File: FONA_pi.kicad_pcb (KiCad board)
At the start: 2 copper layers, 88.4 x 59.1 mm, 35 parts, among them J1 Conn_01x20_Socket, J10 Conn_01x04_Pin, J11 Conn_01x20_Socket, J12 Conn_01x20_Socket, J13 Conn_01x06_Socket, J14 Conn_01x06_Socket, J15 Conn_01x06_Socket, J3 Conn_01x20_Socket, J4 Conn_01x20_Socket, J5 Conn_01x18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

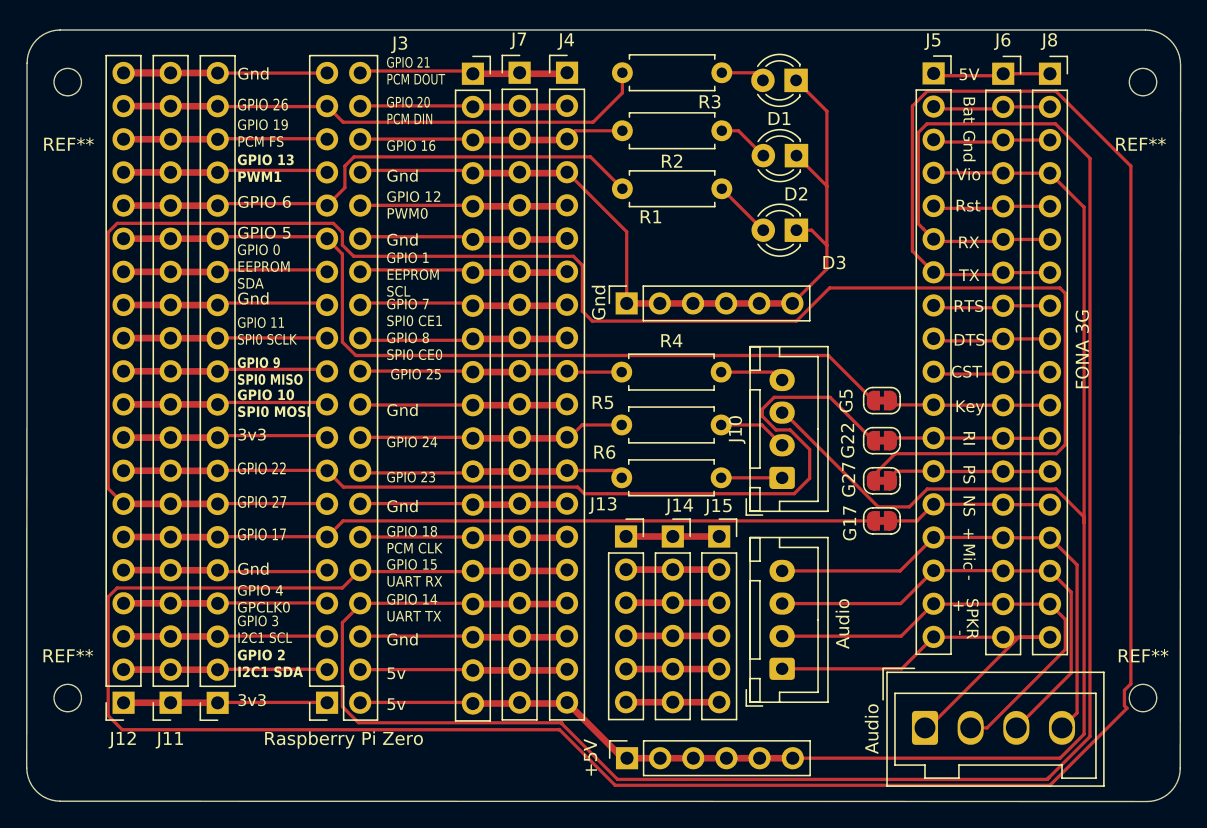
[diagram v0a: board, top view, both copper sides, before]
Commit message: Had to reposition a lot after pulling in from schematic
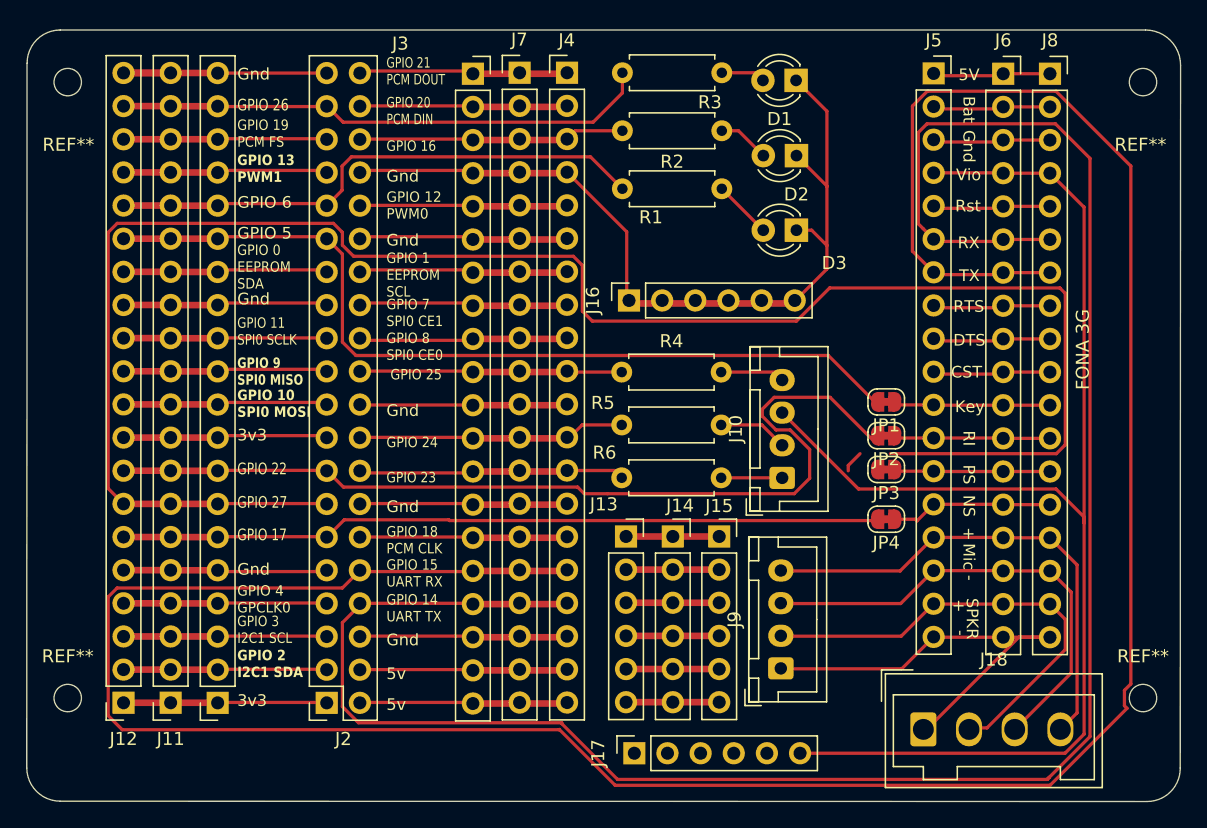
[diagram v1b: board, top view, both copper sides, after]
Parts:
- removed +5V, Gnd: Conn_01x06_Socket, Connector_PinSocket_2.54mm:PinSocket_1x06_P2.54mm_Vertical
- removed Audio: Conn_01x04, Connector_Wago:Wago_734-134_1x04_P3.50mm_Vertical
- removed Audio: Conn_01x04_Pin, Connector_JST:JST_XH_B4B-XH-A_1x04_P2.50mm_Vertical
- removed G17, G22, G27, G5: J2B, Jumper:SolderJumper-2_P1.3mm_Bridged_RoundedPad1.0x1.5mm
- removed Raspberry Pi Zero: Conn_02x20_Odd_Even, Connector_PinSocket_2.54mm:PinSocket_2x20_P2.54mm_Vertical
- added J16: Conn_01x06_Socket, Connector_PinSocket_2.54mm:PinSocket_1x06_P2.54mm_Vertical, F.Cu at (124.6, 78.3)
- added J17: Conn_01x06_Socket, Connector_PinSocket_2.54mm:PinSocket_1x06_P2.54mm_Vertical, F.Cu at (125.0, 113.0)
- added J18: Conn_01x04, Connector_Wago:Wago_734-134_1x04_P3.50mm_Vertical, F.Cu at (147.2, 111.2)
- added J2: Conn_02x20_Odd_Even, Connector_PinSocket_2.54mm:PinSocket_2x20_P2.54mm_Vertical, F.Cu at (101.4, 109.2)
- added J9: Conn_01x04_Pin, Connector_JST:JST_XH_B4B-XH-A_1x04_P2.50mm_Vertical, F.Cu at (136.2, 106.5)
- added JP1: J2B, Jumper:SolderJumper-2_P1.3mm_Bridged_RoundedPad1.0x1.5mm, F.Cu at (144.3, 86.1)
- added JP2: J2B, Jumper:SolderJumper-2_P1.3mm_Bridged_RoundedPad1.0x1.5mm, F.Cu at (144.3, 88.7)
- added JP3: J2B, Jumper:SolderJumper-2_P1.3mm_Bridged_RoundedPad1.0x1.5mm, F.Cu at (144.3, 91.3)
- added JP4: J2B, Jumper:SolderJumper-2_P1.3mm_Bridged_RoundedPad1.0x1.5mm, F.Cu at (144.3, 95.1)
- J8: value unk -> Conn_01x18
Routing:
- net Net-(J10-Pin_3): track 139.3 -> 118.2 mm
- net Net-(J5-Pin_13): track 12.8 -> 11.8 mm
- net Net-(J1-Pin_7): track 145.4 -> 144.7 mm
- net Net-(J5-Pin_14): track 13.0 -> 12.5 mm

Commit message: Fixed DRC violations
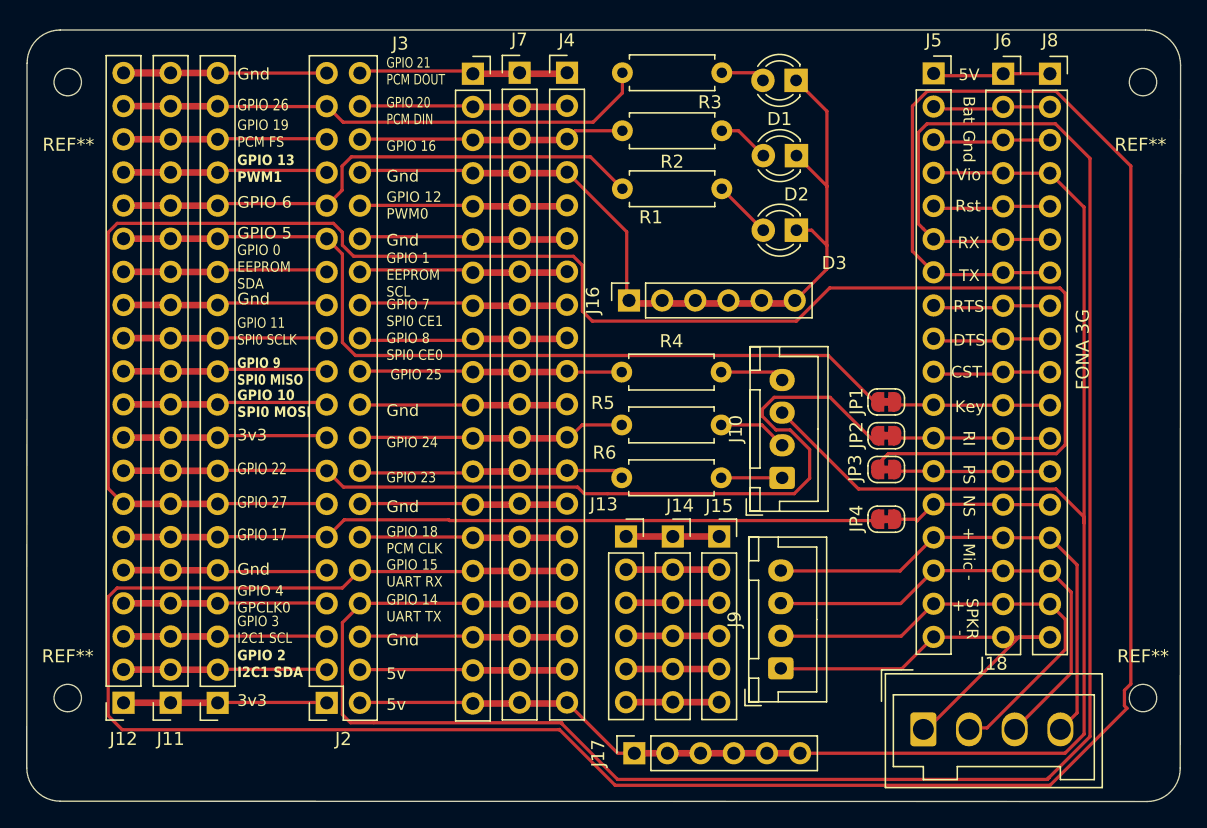
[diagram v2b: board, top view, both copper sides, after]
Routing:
- net Net-(J10-Pin_3): track 118.2 -> 137.6 mm

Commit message: last commit didn't have some saved files that are in this commit
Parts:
- J9 Audio: renamed from J9
- renumbered J16 to GND
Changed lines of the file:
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@@
     (property "ki_keywords" "connector")
     (attr through_hole)
-    (fp_text reference "J9" (at 3.75 -3.55 90) (layer "F.SilkS")
+    (fp_text reference "J9 Audio" (at -3.556 0 180) (layer "F.SilkS")
         (effects (font (size 1 1) (thickness 0.15)))
     )
@@
     (property "ki_keywords" "connector")
     (attr through_hole)
-    (fp_text reference "J16" (at 0 -2.77 90) (layer "F.SilkS")
-        (effects (font (size 1 1) (thickness 0.15)))
-    )
+    (fp_text reference "GND" (at 0 -2.4384 90) (layer "F.SilkS")
+        (effects (font (size 1 1) (thickness 0.15)))
+    )

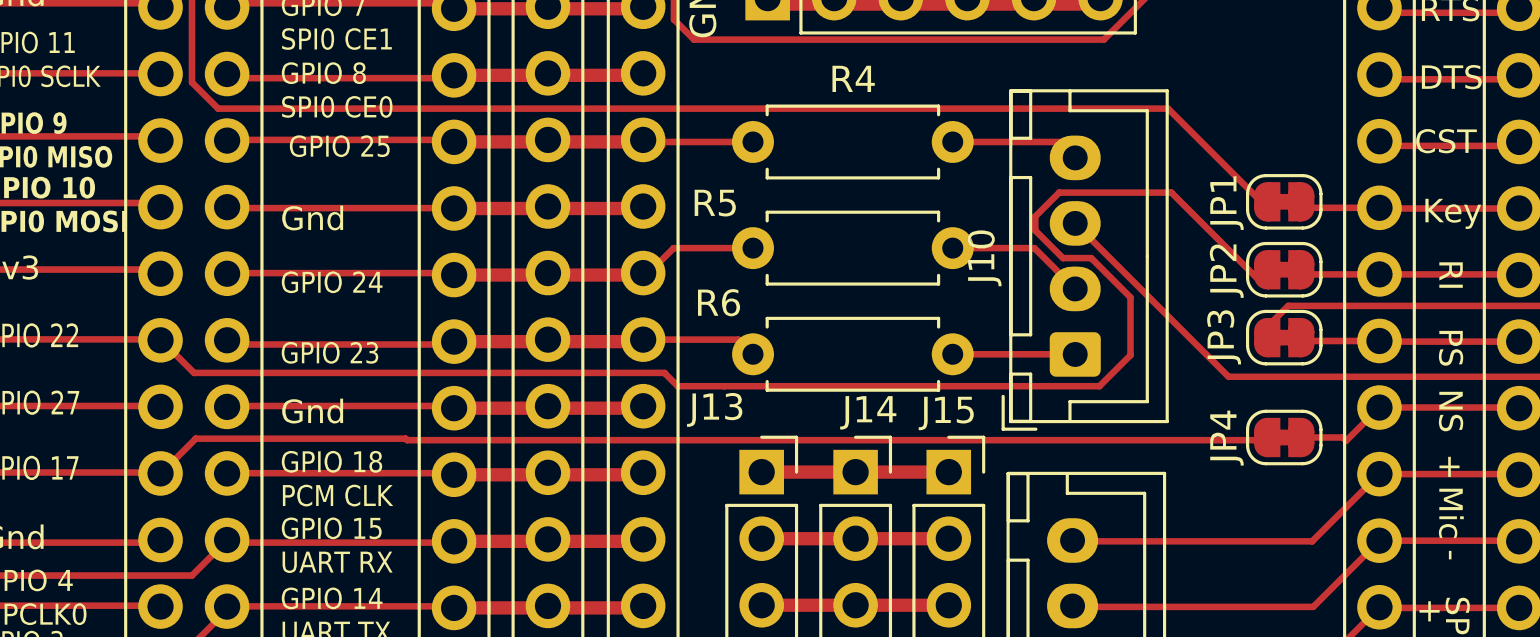
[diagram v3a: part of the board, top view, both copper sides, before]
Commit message: Rearranged jumper pads and tracks
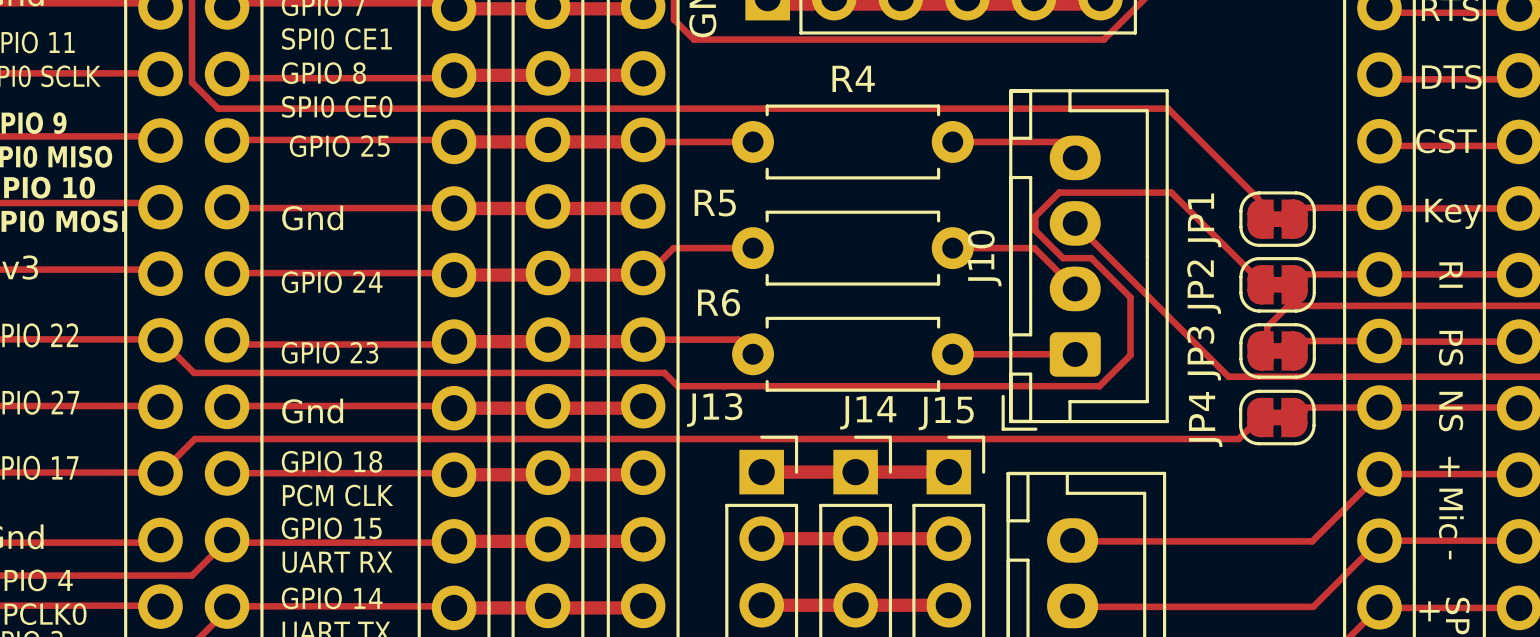
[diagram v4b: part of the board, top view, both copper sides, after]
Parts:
- moved JP4 0.81 mm to (144.1, 94.3)
- moved JP1 0.71 mm to (144.1, 86.8)
- moved JP2 0.63 mm to (144.1, 89.3)
- moved JP3 0.57 mm to (144.1, 91.8)
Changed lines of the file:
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@@
   )
   (footprint "Jumper:SolderJumper-2_P1.3mm_Bridged_RoundedPad1.0x1.5mm" (layer "F.Cu")
-    (at 144.3228 88.6968 180)
+    (at 144.0688 89.272533 180)
     (descr "SMD Solder Jumper, 1x1.5mm, rounded Pads, 0.3mm gap, bridged with 1 copper strip")
     (tags "net tie solder jumper bridged")
@@
     (attr exclude_from_pos_files)
     (net_tie_pad_groups "1, 2")
-    (fp_text reference "JP2" (at 2.286 0.0508 90) (layer "F.SilkS")
-        (effects (font (size 1 1) (thickness 0.15)))
-    )
-    (fp_text value "J2B" (at 0 1.9) (layer "F.Fab")
+    (fp_text reference "JP2" (at 2.8956 0.016933 90) (layer "F.SilkS")
+        (effects (font (size 1 1) (thickness 0.15)))
+    )
+    (fp_text value "J2B" (at 2.4384 1.998133) (layer "F.Fab")
         (effects (font (size 1 1) (thickness 0.15)))
     )
@@
   )
   (footprint "Jumper:SolderJumper-2_P1.3mm_Bridged_RoundedPad1.0x1.5mm" (layer "F.Cu")
-    (at 144.3228 95.0976 180)
+    (at 144.0584 94.3356 180)
     (descr "SMD Solder Jumper, 1x1.5mm, rounded Pads, 0.3mm gap, bridged with 1 copper strip")
     (tags "net tie solder jumper bridged")
@@
     (attr exclude_from_pos_files)
     (net_tie_pad_groups "1, 2")
-    (fp_text reference "JP4" (at 2.286 0.0508 90) (layer "F.SilkS")
-        (effects (font (size 1 1) (thickness 0.15)))
-    )
-    (fp_text value "J2B" (at 2.6416 1.524) (layer "F.Fab")
+    (fp_text reference "JP4" (at 2.8344 0 90) (layer "F.SilkS")
+        (effects (font (size 1 1) (thickness 0.15)))
+    )
+    (fp_text value "J2B" (at -0.874 -1.8796) (layer "F.Fab")
         (effects (font (size 1 1) (thickness 0.15)))
     )
@@
   )
   (footprint "Jumper:SolderJumper-2_P1.3mm_Bridged_RoundedPad1.0x1.5mm" (layer "F.Cu")
-    (at 144.3228 86.106 180)
+    (at 144.0688 86.7664 180)
     (descr "SMD Solder Jumper, 1x1.5mm, rounded Pads, 0.3mm gap, bridged with 1 copper strip")
     (tags "net tie solder jumper bridged")
@@
     (attr exclude_from_pos_files)
     (net_tie_pad_groups "1, 2")
-    (fp_text reference "JP1" (at 2.286 0.0508 90) (layer "F.SilkS")
+    (fp_text reference "JP1" (at 2.8852 0.0508 90) (layer "F.SilkS")
         (effects (font (size 1 1) (thickness 0.15)))
     )
@@
   )
   (footprint "Jumper:SolderJumper-2_P1.3mm_Bridged_RoundedPad1.0x1.5mm" (layer "F.Cu")
-    (at 144.3228 91.2876 180)
+    (at 144.0688 91.7956 180)
     (descr "SMD Solder Jumper, 1x1.5mm, rounded Pads, 0.3mm gap, bridged with 1 copper strip")
     (tags "net tie solder jumper bridged")
@@
     (attr exclude_from_pos_files)
     (net_tie_pad_groups "1, 2")
-    (fp_text reference "JP3" (at 2.3876 0.1016 90) (layer "F.SilkS")
-        (effects (font (size 1 1) (thickness 0.15)))
-    )
-    (fp_text value "J2B" (at 0 1.9) (layer "F.Fab")
+    (fp_text reference "JP3" (at 2.8956 0 90) (layer "F.SilkS")
+        (effects (font (size 1 1) (thickness 0.15)))
+    )
+    (fp_text value "J2B" (at -1.9304 -0.762) (layer "F.Fab")
         (effects (font (size 1 1) (thickness 0.15)))
     )
@@
   (segment (start 92.8116 101.5146) (end 101.4476 101.5146) (width 0.25) (layer "F.Cu") (net 3))
   (segment (start 89.496 96.4692) (end 89.4868 96.46) (width 0.508) (layer "F.Cu") (net 4))
-  (segment (start 143.5712 95.1992) (end 143.6728 95.0976) (width 0.25) (layer "F.Cu") (net 4))
-  (segment (start 110.8014 95.1418) (end 110.8588 95.1992) (width 0.25) (layer "F.Cu") (net 4))
+  (segment (start 102.7618 95.155) (end 101.4476 96.4692) (width 0.25) (layer "F.Cu") (net 4))
   (segment (start 85.8774 96.46) (end 89.4868 96.46) (width 0.508) (layer "F.Cu") (net 4))
-  (segment (start 102.7912 95.1418) (end 110.8014 95.1418) (width 0.25) (layer "F.Cu") (net 4))
   (segment (start 92.8116 96.4346) (end 101.4476 96.4346) (width 0.25) (layer "F.Cu") (net 4))
   (segment (start 93.091 96.4692) (end 89.496 96.4692) (width 0.508) (layer "F.Cu") (net 4))
-  (segment (start 101.473 96.46) (end 102.7912 95.1418) (width 0.25) (layer "F.Cu") (net 4))
-  (segment (start 110.8588 95.1992) (end 143.5712 95.1992) (width 0.25) (layer "F.Cu") (net 4))
+  (segment (start 142.589 95.155) (end 102.7618 95.155) (width 0.25) (layer "F.Cu") (net 4))
+  (segment (start 143.4084 94.3356) (end 142.589 95.155) (width 0.25) (layer "F.Cu") (net 4))
   (segment (start 138.4554 89.751099) (end 138.4554 91.959573) (width 0.25) (layer "F.Cu") (net 5))
   (segment (start 140.0194 85.7546) (end 135.735499 85.7546) (width 0.25) (layer "F.Cu") (net 5))
@@
   (segment (start 156.8704 91.44) (end 153.2864 91.44) (width 0.25) (layer "F.Cu") (net 43))
   (segment (start 153.2864 91.44) (end 147.9804 91.44) (width 0.25) (layer "F.Cu") (net 43))
-  (segment (start 146.558 95.0976) (end 144.9728 95.0976) (width 0.25) (layer "F.Cu") (net 44))
+  (segment (start 144.7084 94.3356) (end 145.0894 93.9546) (width 0.25) (layer "F.Cu") (net 44))
   (segment (start 153.2864 93.98) (end 156.8704 93.98) (width 0.25) (layer "F.Cu") (net 44))
   (segment (start 147.955 93.9546) (end 153.261 93.9546) (width 0.25) (layer "F.Cu") (net 44))
-  (segment (start 146.685 95.2246) (end 146.558 95.0976) (width 0.25) (layer "F.Cu") (net 44))
+  (segment (start 145.0894 93.9546) (end 147.955 93.9546) (width 0.25) (layer "F.Cu") (net 44))
   (segment (start 153.261 93.9546) (end 153.2864 93.98) (width 0.25) (layer "F.Cu") (net 44))
-  (segment (start 147.955 93.9546) (end 146.685 95.2246) (width 0.25) (layer "F.Cu") (net 44))
   (segment (start 112.649 93.98) (end 116.2304 93.98) (width 0.508) (layer "F.Cu") (net 45))
   (segment (start 116.2304 93.98) (end 119.8626 93.98) (width 0.508) (layer "F.Cu") (net 45))
